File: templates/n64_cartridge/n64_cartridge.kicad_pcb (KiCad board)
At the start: 2 copper layers, 100 x 60 mm, 3 parts, among them J1 N64_Cartridge_Bus

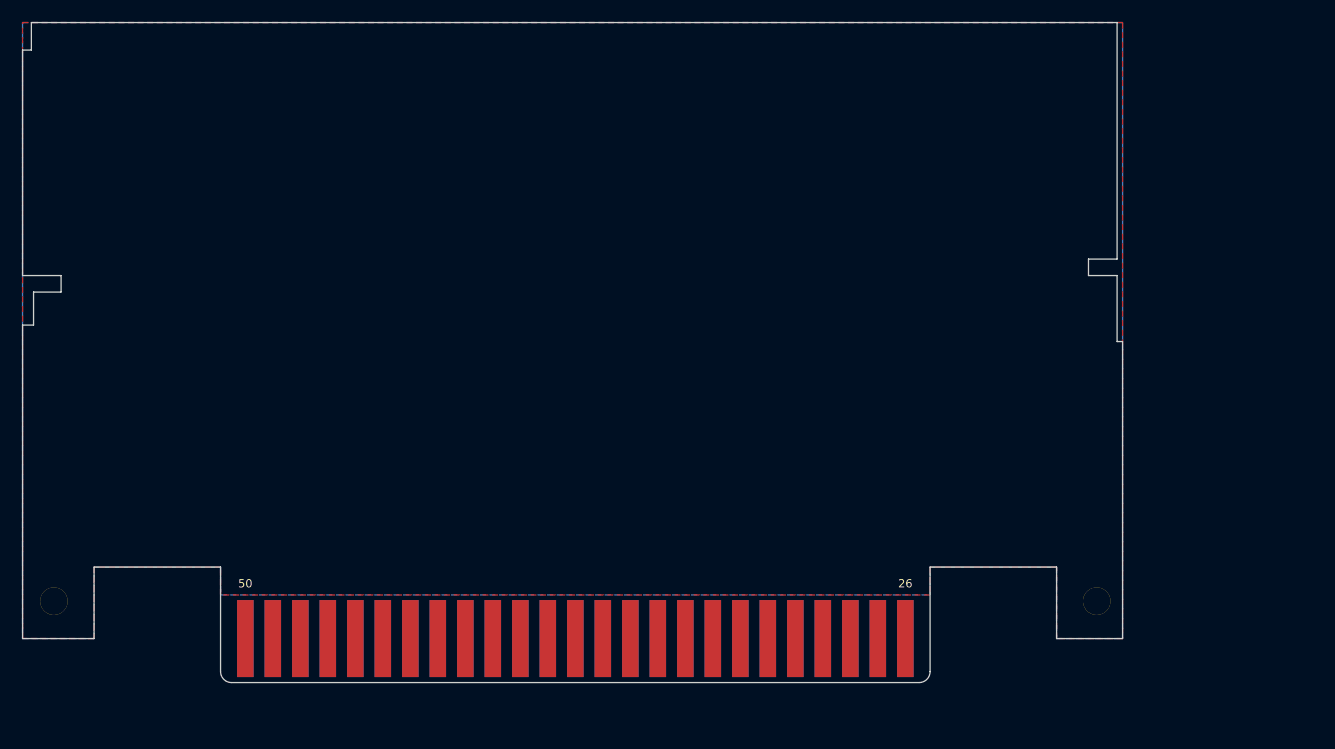
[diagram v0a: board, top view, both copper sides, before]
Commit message: Translate PCB so that card edge footprint has round number coordinates
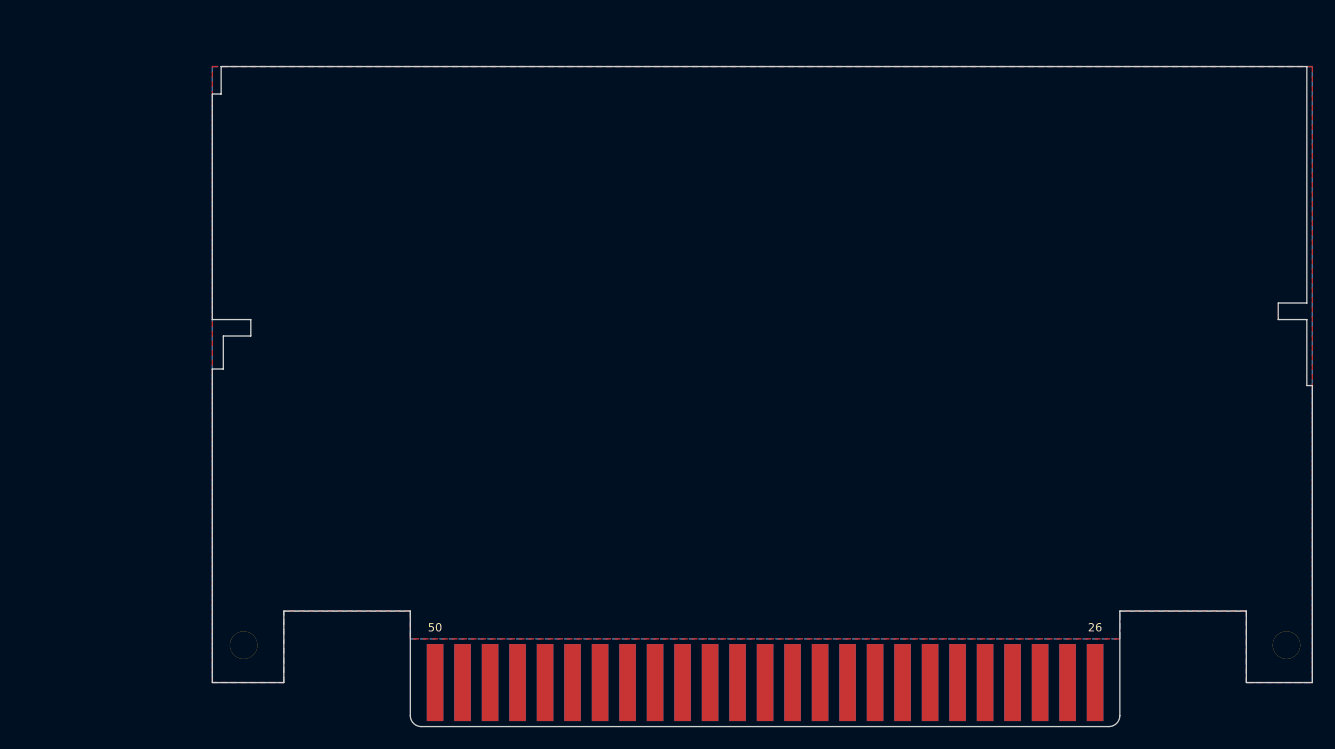
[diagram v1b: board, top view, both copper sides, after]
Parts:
- moved J1 17.7 mm to (150.0, 130.0)
- moved REF** 17.7 mm to (197.4, 126.6)
- moved REF** 17.7 mm to (102.6, 126.6)
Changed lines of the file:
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@@
   (page A4)
   (layers
-    (0 F.Cu signal)
-    (31 B.Cu signal)
+    (0 F.Cu signal hide)
+    (31 B.Cu signal hide)
     (32 B.Adhes user)
     (33 F.Adhes user)
@@
     (solder_mask_min_width 0.3)
     (aux_axis_origin 0 0)
-    (visible_elements 7FFFFF7F)
+    (grid_origin 150 123.5)
+    (visible_elements 7FFFF77F)
     (pcbplotparams
       (layerselection 0x010fc_ffffffff)
@@
   )
   (module n64_cartridge:N64_Cartridge_Edge locked (layer F.Cu)
-    (at 132.75 126)
+    (at 150 130)
     (attr virtual)
     (fp_text reference J1 (at 0 5.4) (layer F.SilkS) hide
@@
   )
   (module MountingHole:MountingHole_2.5mm_Pad locked (layer F.Cu)
-    (at 180.15 122.6)
+    (at 197.4 126.6)
     (descr "Mounting Hole 2.5mm")
     (tags "mounting hole 2.5mm")
@@
   )
   (module MountingHole:MountingHole_2.5mm_Pad locked (layer F.Cu)
-    (at 85.35 122.6)
+    (at 102.6 126.6)
     (descr "Mounting Hole 2.5mm")
     (tags "mounting hole 2.5mm")
@@
       (net 1 GND) (zone_connect 2))
   )
-  (gr_arc (start 164 129) (end 164 130) (angle -90) (layer Edge.Cuts) (width 0.1))
-  (gr_arc (start 101.5 129) (end 101.5 130) (angle 90) (layer Edge.Cuts) (width 0.1))
-  (gr_text 25 (at 102.775 121) (layer B.SilkS)
+  (gr_arc (start 181.25 133) (end 181.25 134) (angle -90) (layer Edge.Cuts) (width 0.1))
+  (gr_arc (start 118.75 133) (end 118.75 134) (angle 90) (layer Edge.Cuts) (width 0.1))
+  (gr_text 25 (at 120.025 125) (layer B.SilkS)
     (effects (font (size 0.75 0.75) (thickness 0.15)) (justify mirror))
   )
-  (gr_text 26 (at 162.75 121) (layer F.SilkS)
+  (gr_text 26 (at 180 125) (layer F.SilkS)
     (effects (font (size 0.75 0.75) (thickness 0.15)))
   )
-  (gr_text 1 (at 162.775 121) (layer B.SilkS)
+  (gr_text 1 (at 180.025 125) (layer B.SilkS)
     (effects (font (size 0.75 0.75) (thickness 0.15)) (justify mirror))
   )
-  (gr_text 50 (at 102.75 121) (layer F.SilkS)
+  (gr_text 50 (at 120 125) (layer F.SilkS)
     (effects (font (size 0.75 0.75) (thickness 0.15)))
   )
-  (gr_line (start 176.5 119.5) (end 176.5 126) (layer Edge.Cuts) (width 0.1))
-  (gr_line (start 83.3 72.5) (end 83.3 70) (layer Edge.Cuts) (width 0.1))
-  (gr_line (start 82.5 72.5) (end 83.3 72.5) (layer Edge.Cuts) (width 0.1))
-  (gr_line (start 182 70) (end 182 91.5) (layer Edge.Cuts) (width 0.1))
-  (gr_line (start 182 91.5) (end 179.4 91.5) (layer Edge.Cuts) (width 0.1))
-  (gr_line (start 182 93) (end 179.4 93) (layer Edge.Cuts) (width 0.1))
-  (gr_line (start 179.4 93) (end 179.4 91.5) (layer Edge.Cuts) (width 0.1))
-  (gr_line (start 182 93) (end 182 99) (layer Edge.Cuts) (width 0.1))
-  (gr_line (start 83.3 70) (end 182 70) (layer Edge.Cuts) (width 0.1))
-  (gr_line (start 82.5 93) (end 82.5 72.5) (layer Edge.Cuts) (width 0.1))
-  (gr_line (start 86 93) (end 82.5 93) (layer Edge.Cuts) (width 0.1))
-  (gr_line (start 86 94.5) (end 86 93) (layer Edge.Cuts) (width 0.1))
-  (gr_line (start 83.5 94.5) (end 86 94.5) (layer Edge.Cuts) (width 0.1))
-  (gr_line (start 83.5 97.5) (end 83.5 94.5) (layer Edge.Cuts) (width 0.1))
-  (gr_line (start 82.5 97.5) (end 83.5 97.5) (layer Edge.Cuts) (width 0.1))
-  (gr_line (start 182.5 99) (end 182 99) (layer Edge.Cuts) (width 0.1))
-  (gr_line (start 182.5 126) (end 182.5 99) (layer Edge.Cuts) (width 0.1))
-  (gr_line (start 182.5 126) (end 176.5 126) (layer Edge.Cuts) (width 0.1))
-  (gr_line (start 176.5 119.5) (end 165 119.5) (layer Edge.Cuts) (width 0.1))
-  (gr_line (start 165 129) (end 165 119.5) (layer Edge.Cuts) (width 0.1))
-  (gr_line (start 82.5 126) (end 82.5 97.5) (layer Edge.Cuts) (width 0.1))
-  (gr_line (start 89 126) (end 82.5 126) (layer Edge.Cuts) (width 0.1))
-  (gr_line (start 89 119.5) (end 89 126) (layer Edge.Cuts) (width 0.1))
-  (gr_line (start 100.5 119.5) (end 89 119.5) (layer Edge.Cuts) (width 0.1))
-  (gr_line (start 100.5 129) (end 100.5 119.5) (layer Edge.Cuts) (width 0.1))
-  (gr_line (start 164 130) (end 101.5 130) (layer Edge.Cuts) (width 0.1))
+  (gr_line (start 193.75 123.5) (end 193.75 130) (layer Edge.Cuts) (width 0.1))
+  (gr_line (start 100.55 76.5) (end 100.55 74) (layer Edge.Cuts) (width 0.1))
+  (gr_line (start 99.75 76.5) (end 100.55 76.5) (layer Edge.Cuts) (width 0.1))
+  (gr_line (start 199.25 74) (end 199.25 95.5) (layer Edge.Cuts) (width 0.1))
+  (gr_line (start 199.25 95.5) (end 196.65 95.5) (layer Edge.Cuts) (width 0.1))
+  (gr_line (start 199.25 97) (end 196.65 97) (layer Edge.Cuts) (width 0.1))
+  (gr_line (start 196.65 97) (end 196.65 95.5) (layer Edge.Cuts) (width 0.1))
+  (gr_line (start 199.25 97) (end 199.25 103) (layer Edge.Cuts) (width 0.1))
+  (gr_line (start 100.55 74) (end 199.25 74) (layer Edge.Cuts) (width 0.1))
+  (gr_line (start 99.75 97) (end 99.75 76.5) (layer Edge.Cuts) (width 0.1))
+  (gr_line (start 103.25 97) (end 99.75 97) (layer Edge.Cuts) (width 0.1))
+  (gr_line (start 103.25 98.5) (end 103.25 97) (layer Edge.Cuts) (width 0.1))
+  (gr_line (start 100.75 98.5) (end 103.25 98.5) (layer Edge.Cuts) (width 0.1))
+  (gr_line (start 100.75 101.5) (end 100.75 98.5) (layer Edge.Cuts) (width 0.1))
+  (gr_line (start 99.75 101.5) (end 100.75 101.5) (layer Edge.Cuts) (width 0.1))
+  (gr_line (start 199.75 103) (end 199.25 103) (layer Edge.Cuts) (width 0.1))
+  (gr_line (start 199.75 130) (end 199.75 103) (layer Edge.Cuts) (width 0.1))
+  (gr_line (start 199.75 130) (end 193.75 130) (layer Edge.Cuts) (width 0.1))
+  (gr_line (start 193.75 123.5) (end 182.25 123.5) (layer Edge.Cuts) (width 0.1))
+  (gr_line (start 182.25 133) (end 182.25 123.5) (layer Edge.Cuts) (width 0.1))
+  (gr_line (start 99.75 130) (end 99.75 101.5) (layer Edge.Cuts) (width 0.1))
+  (gr_line (start 106.25 130) (end 99.75 130) (layer Edge.Cuts) (width 0.1))
+  (gr_line (start 106.25 123.5) (end 106.25 130) (layer Edge.Cuts) (width 0.1))
+  (gr_line (start 117.75 123.5) (end 106.25 123.5) (layer Edge.Cuts) (width 0.1))
+  (gr_line (start 117.75 133) (end 117.75 123.5) (layer Edge.Cuts) (width 0.1))
+  (gr_line (start 181.25 134) (end 118.75 134) (layer Edge.Cuts) (width 0.1))
   (zone (net 1) (net_name GND) (layer F.Cu) (hatch edge 0.508)
     (connect_pads (clearance 0.2))
@@
     (polygon
       (pts
-        (xy 182.5 70) (xy 182.5 126) (xy 176.5 126) (xy 176.5 119.5) (xy 165 119.5)
-        (xy 165 122.03) (xy 100.5 122.03) (xy 100.5 119.5) (xy 89 119.5) (xy 89 126)
-        (xy 82.51 125.99) (xy 82.5 70)
+        (xy 199.75 74) (xy 199.75 130) (xy 193.75 130) (xy 193.75 123.5) (xy 182.25 123.5)
+        (xy 182.25 126.03) (xy 117.75 126.03) (xy 117.75 123.5) (xy 106.25 123.5) (xy 106.25 130)
+        (xy 99.76 129.99) (xy 99.75 74)
       )
     )
@@
     (polygon
       (pts
-        (xy 88.9 119.5) (xy 82.5 119.5) (xy 82.5 126) (xy 89 126) (xy 89 119.5)
+        (xy 106.15 123.5) (xy 99.75 123.5) (xy 99.75 130) (xy 106.25 130) (xy 106.25 123.5)
       )
     )
@@
     (polygon
       (pts
-        (xy 89 126) (xy 89 119.5) (xy 82.5 119.5) (xy 82.5 126)
+        (xy 106.25 130) (xy 106.25 123.5) (xy 99.75 123.5) (xy 99.75 130)
       )
     )
@@
     (polygon
       (pts
-        (xy 176.5 119.5) (xy 182.5 119.5) (xy 182.5 126) (xy 176.5 126)
+        (xy 193.75 123.5) (xy 199.75 123.5) (xy 199.75 130) (xy 193.75 130)
       )
     )
@@
     (polygon
       (pts
-        (xy 176.5 119.5) (xy 182.5 119.5) (xy 182.5 126) (xy 176.5 126)
+        (xy 193.75 123.5) (xy 199.75 123.5) (xy 199.75 130) (xy 193.75 130)
       )
     )
@@
     (polygon
       (pts
-        (xy 100.5 119.5) (xy 100.51 122.03) (xy 165 122.03) (xy 165 119.5) (xy 176.5 119.5)
-        (xy 176.5 126) (xy 182.5 126) (xy 182.5 70) (xy 82.5 70) (xy 82.5 126)
-        (xy 89 126) (xy 89 119.5)
+        (xy 117.75 123.5) (xy 117.76 126.03) (xy 182.25 126.03) (xy 182.25 123.5) (xy 193.75 123.5)
+        (xy 193.75 130) (xy 199.75 130) (xy 199.75 74) (xy 99.75 74) (xy 99.75 130)
+        (xy 106.25 130) (xy 106.25 123.5)
       )
     )
@@
     (polygon
       (pts
-        (xy 165 130) (xy 100.5 130) (xy 100.5 123) (xy 165 123)
+        (xy 182.25 134) (xy 117.75 134) (xy 117.75 127) (xy 182.25 127)
       )
     )
@@
     (polygon
       (pts
-        (xy 165 130) (xy 100.5 130) (xy 100.5 123) (xy 165 123)
+        (xy 182.25 134) (xy 117.75 134) (xy 117.75 127) (xy 182.25 127)
       )
     )
@@
     (polygon
       (pts
-        (xy 182.5 119.5) (xy 179 119.5) (xy 179 100) (xy 182.5 100)
+        (xy 199.75 123.5) (xy 196.25 123.5) (xy 196.25 104) (xy 199.75 104)
       )
     )
@@
     (polygon
       (pts
-        (xy 182.5 119.5) (xy 179 119.5) (xy 179 100) (xy 182.5 100)
+        (xy 199.75 123.5) (xy 196.25 123.5) (xy 196.25 104) (xy 199.75 104)
       )
     )
@@
     (polygon
       (pts
-        (xy 86 119.5) (xy 82.5 119.5) (xy 82.5 98.5) (xy 86 98.5)
+        (xy 103.25 123.5) (xy 99.75 123.5) (xy 99.75 102.5) (xy 103.25 102.5)
       )
     )
@@
     (polygon
       (pts
-        (xy 86 119.5) (xy 82.5 119.5) (xy 82.5 98.5) (xy 86 98.5)
-      )
-    )
+        (xy 103.25 123.5) (xy 99.75 123.5) (xy 99.75 102.5) (xy 103.25 102.5)
+      )
+    )
